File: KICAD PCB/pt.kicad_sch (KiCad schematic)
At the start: 3 parts

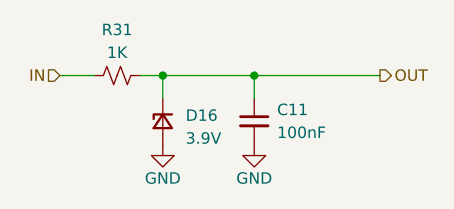
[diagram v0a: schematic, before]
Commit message: moved to stm32cube vscode extension, v2.0 purchased
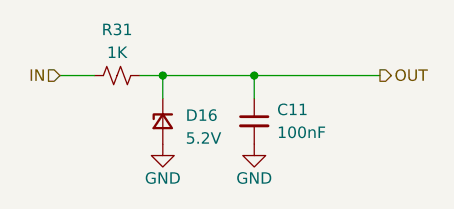
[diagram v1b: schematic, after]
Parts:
- D16: value 3.9V -> 5.2V
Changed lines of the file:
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@@
 			)
 		)
-		(property "Value" "3.9V"
+		(property "Value" "5.2V"
 			(at 57.15 93.345 90)
 			(effects
@@
 			)
 		)
-		(property "Datasheet" "https://mm.digikey.com/Volume0/opasdata/d220001/medias/docus/4849/DS_31_BZT52C2V4LP-BZT52C39LP.pdf"
+		(property "Datasheet" "https://jlcpcb.com/api/file/downloadByFileSystemAccessId/8588918152696225792"
 			(at 54.61 91.44 90)
 			(effects
@@
 			)
 		)
-		(property "Description" "BZT52C3V6LP-7"
+		(property "Description" "BZX884-B5V6"
 			(at 54.61 91.44 0)
 			(effects
